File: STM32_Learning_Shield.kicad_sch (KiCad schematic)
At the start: 8 parts, among them J1 Power, J2 Digital/PWM, J3 Analog, J4 Digital/PWM, J7 Conn_01x03

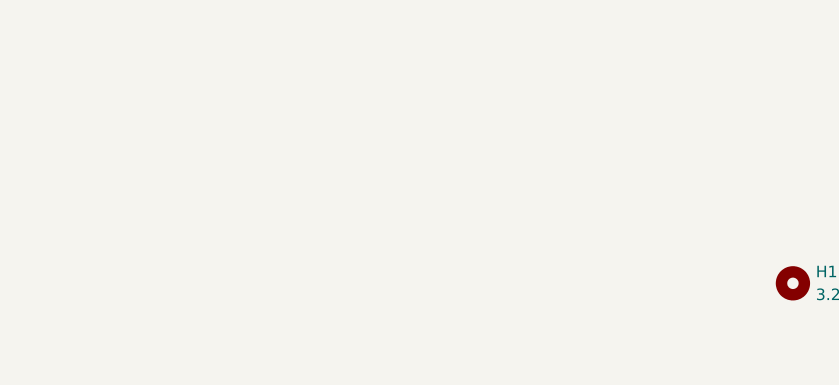
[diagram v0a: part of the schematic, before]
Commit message: Add Fiducials
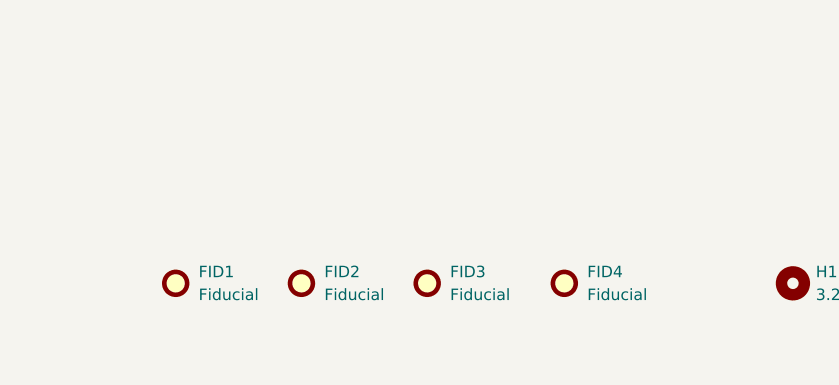
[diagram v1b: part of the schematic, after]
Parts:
- added FID1, FID2, FID3, FID4: Fiducial, Fiducial:Fiducial_1mm_Mask3mm, symbol Mechanical:Fiducial
